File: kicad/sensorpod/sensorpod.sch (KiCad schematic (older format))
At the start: 48 parts, among them M1 MOTOR, P1 HEADER_(8_WAY), Q1 IRFML8244TRPBF

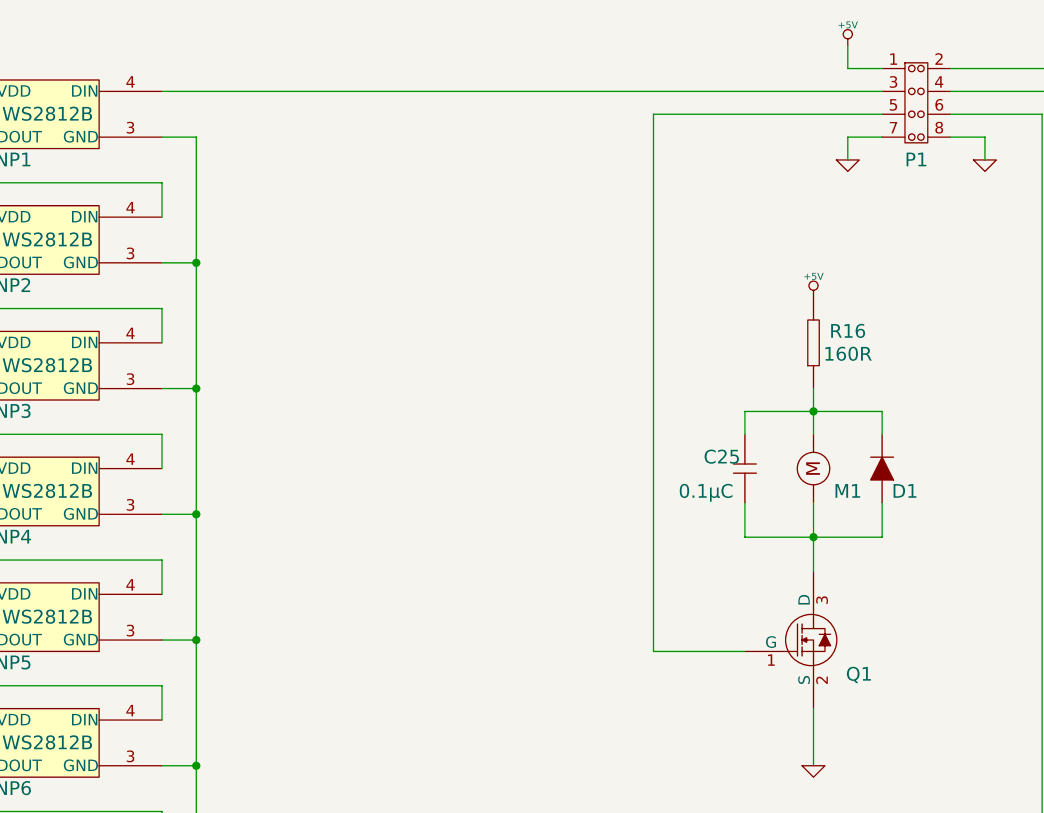
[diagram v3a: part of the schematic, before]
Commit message: Swap a few cable pins
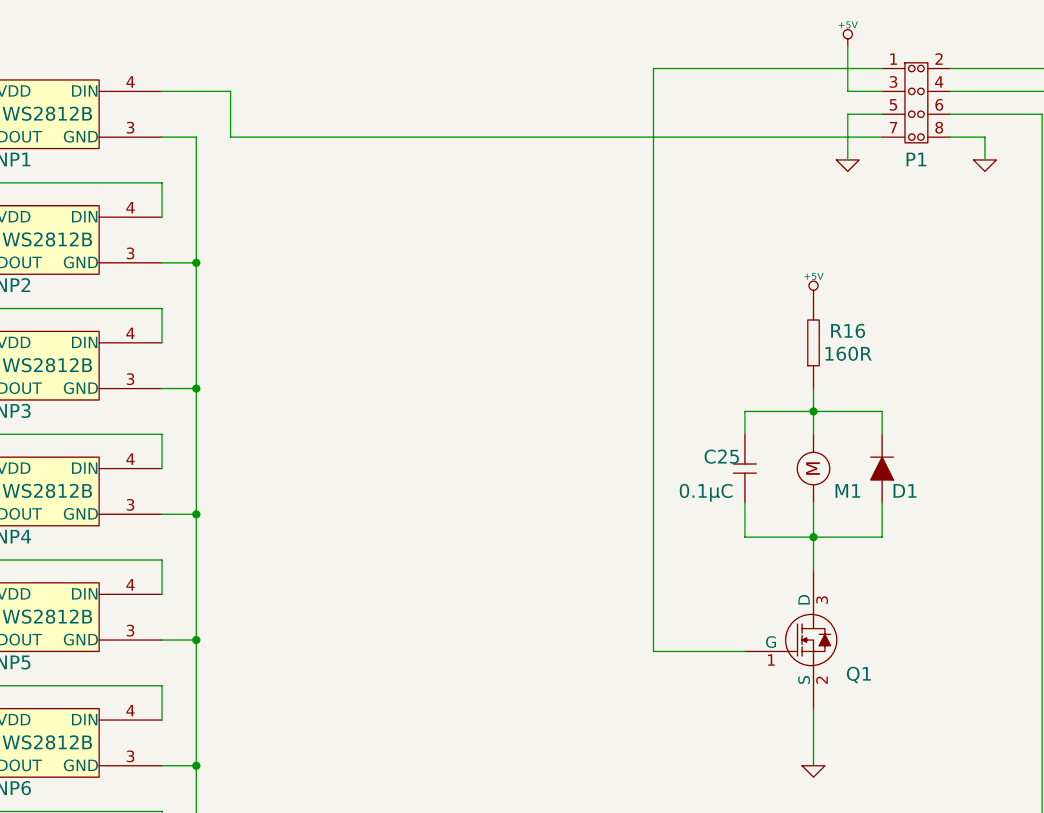
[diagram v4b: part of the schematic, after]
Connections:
- net +5V: now also P1.3; no longer P1.1
- net GND: now also P1.5; no longer P1.7
- net at NP1.4 (DIN): now also P1.7; no longer P1.3
- net at Q1.1 (G): now also P1.1; no longer P1.5
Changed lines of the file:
@@
 Sheet 1 1
 Title ""
-Date "22 feb 2016"
+Date "23 feb 2016"
 Rev ""
 Comp ""
@@
 	1    0    0    -1
 $EndComp
-Wire Wire Line
-	5300 900  5150 900
-Wire Wire Line
-	5150 900  5150 800
 $Comp
 L GND #PWR029
@@
 $EndComp
 Wire Wire Line
-	5600 1200 5750 1200
-Wire Wire Line
 	5750 1200 5750 1300
 Wire Wire Line
-	2150 1000 5300 1000
-Wire Wire Line
 	6100 4800 6100 1000
 Wire Wire Line
-	6100 1000 5600 1000
-Wire Wire Line
 	6000 4900 6000 1100
-Wire Wire Line
-	6000 1100 5600 1100
-Wire Wire Line
-	5600 900  6200 900
 Wire Wire Line
 	6200 900  6200 2500
@@
 $EndComp
 Wire Wire Line
-	5300 1200 5150 1200
-Wire Wire Line
-	5150 1200 5150 1300
+	5150 1100 5150 1300
 $Comp
 L IRFML8244TRPBF Q1
@@
 	5000 3700 5000 3950
 Wire Wire Line
-	4700 3450 4300 3450
-Wire Wire Line
-	4300 3450 4300 1100
-Wire Wire Line
-	4300 1100 5300 1100
+	4300 3450 4700 3450
+Wire Wire Line
+	4300 900  4300 3450
 $Comp
 L MOTOR M1
@@
 	7650 5350 7900 5350
 Connection ~ 7900 5350
+Wire Wire Line
+	4300 900  5300 900
+Wire Wire Line
+	5300 1000 5150 1000
+Wire Wire Line
+	5150 1000 5150 800
+Wire Wire Line
+	5150 1100 5300 1100
+Wire Wire Line
+	5300 1200 2450 1200
+Wire Wire Line
+	2450 1200 2450 1000
+Wire Wire Line
+	2450 1000 2150 1000
+Wire Wire Line
+	5600 1200 5750 1200
+Wire Wire Line
+	6000 1100 5600 1100
+Wire Wire Line
+	6100 1000 5600 1000
+Wire Wire Line
+	5600 900  6200 900
 $EndSCHEMATC

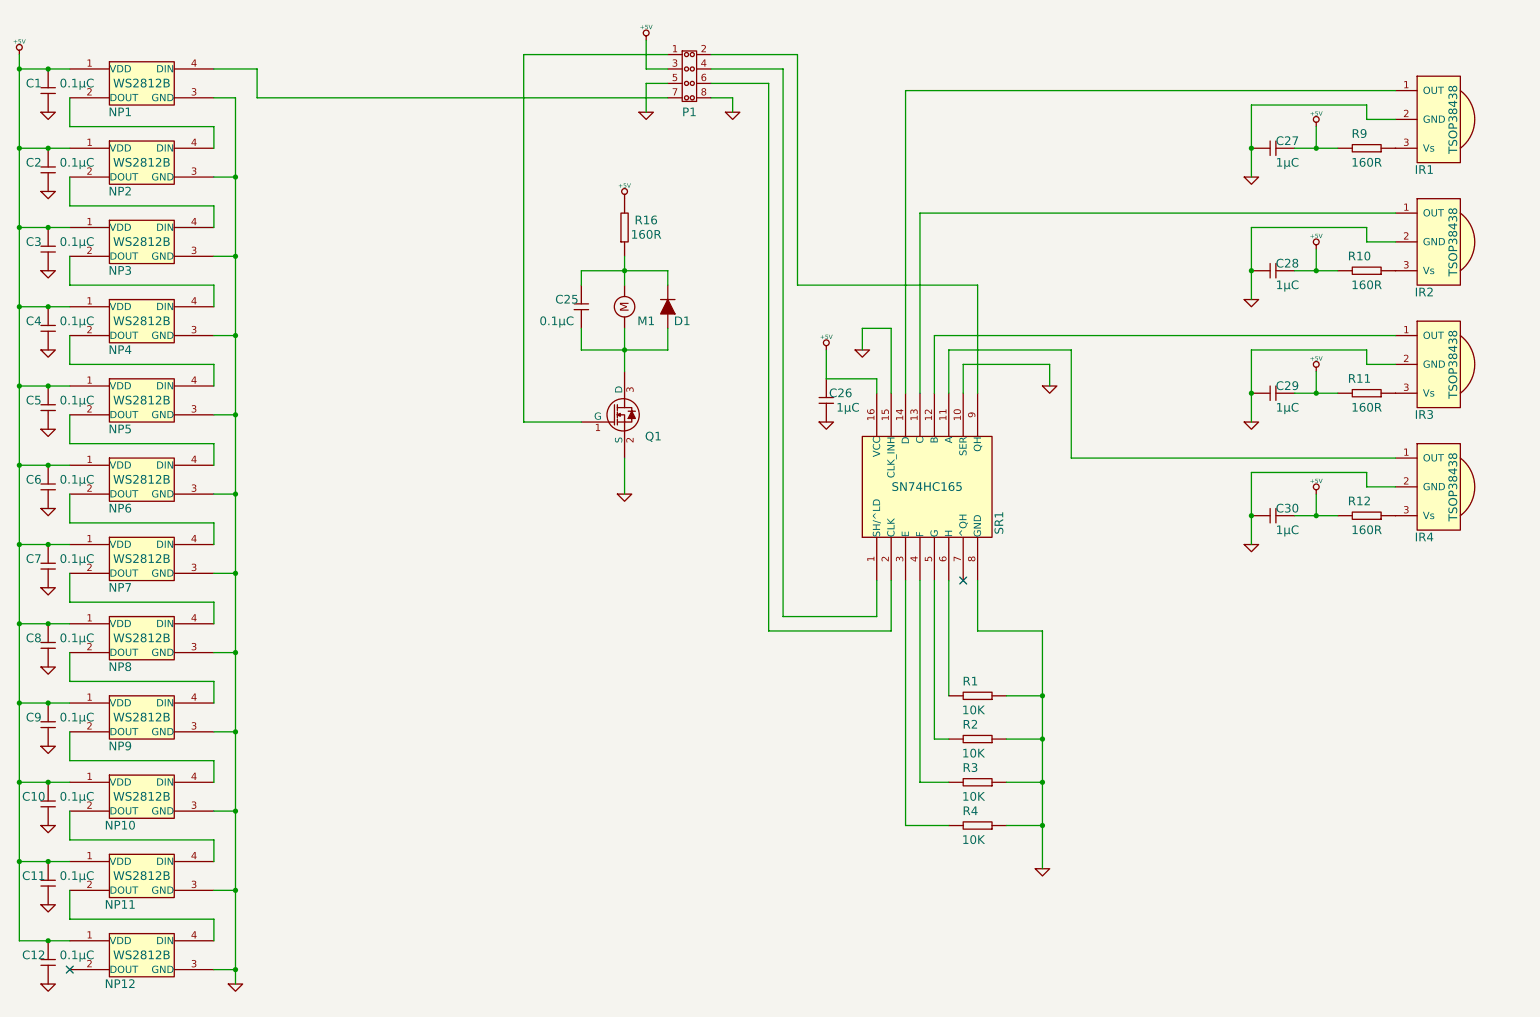
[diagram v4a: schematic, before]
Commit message: Updated sensorpod schematic and PCB to fit into Serpac C9 enclosure
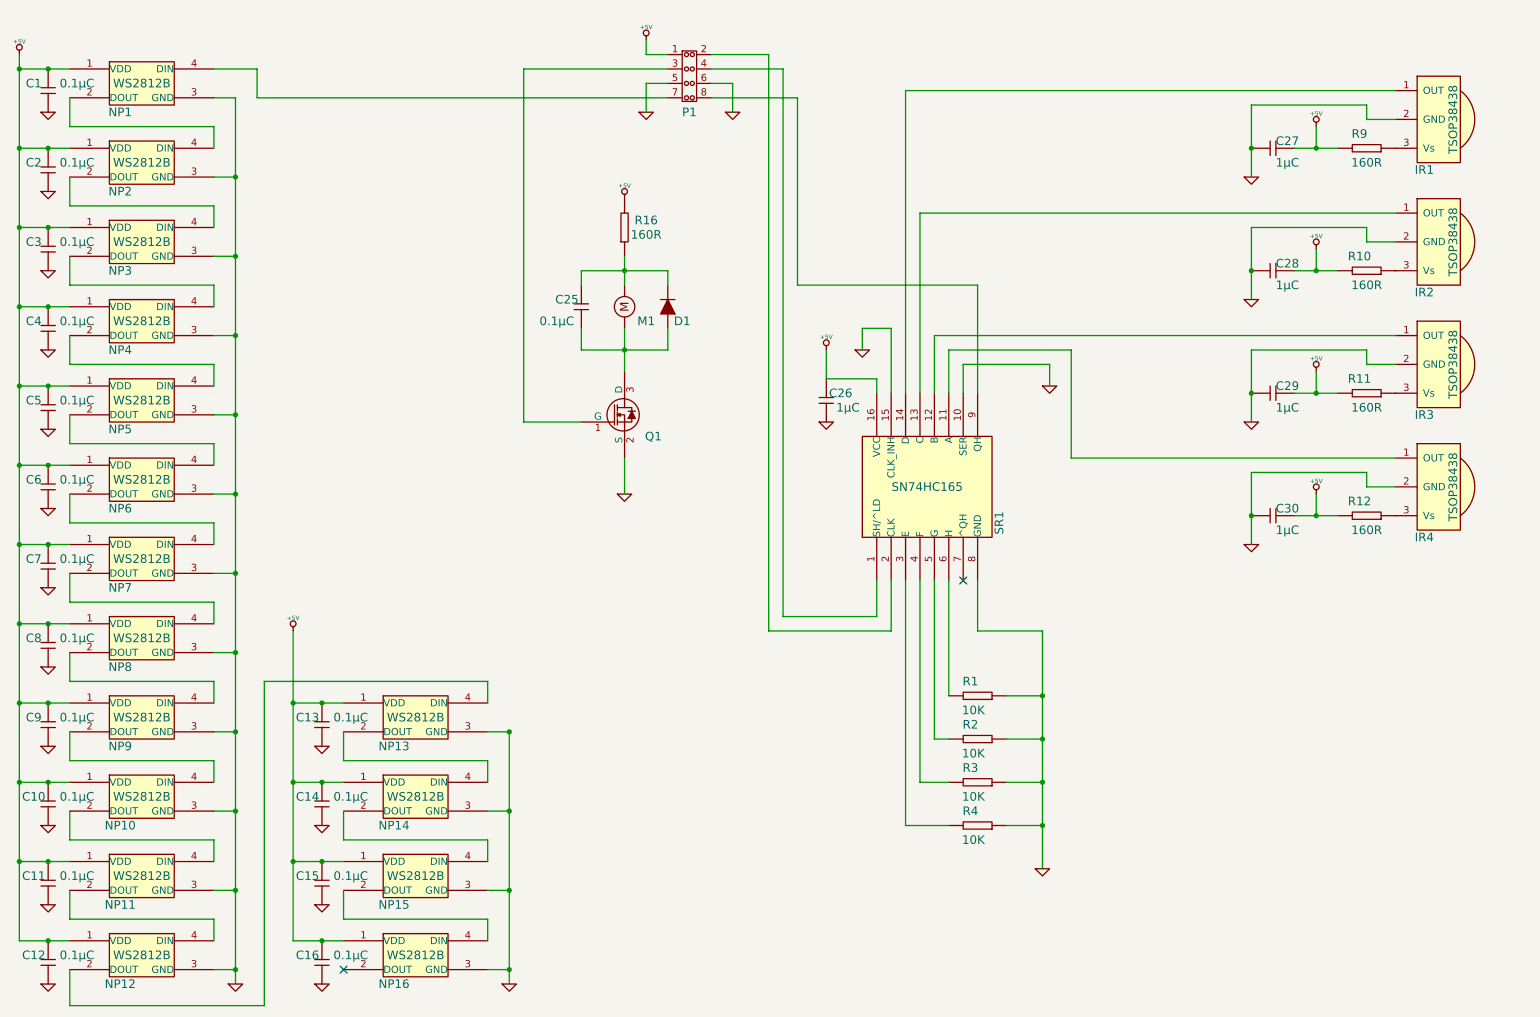
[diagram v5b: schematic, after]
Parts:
- added C13, C14, C15, C16: GENERIC_CAPACITOR, 0805, symbol GENERIC_CAPACITOR
- added NP13, NP14, NP15, NP16: WS2812B, 5050, symbol WS2812B
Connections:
- net +5V: now also P1.1, C13.1, C14.1, C15.1, C16.1, NP13.1 (VDD), NP14.1 (VDD), NP15.1 (VDD), NP16.1 (VDD); no longer P1.3
- net GND: now also P1.6, C13.2, C14.2, C15.2, C16.2, NP13.3 (GND), NP14.3 (GND), NP15.3 (GND), NP16.3 (GND); no longer P1.8
- net at NP12.2 (DOUT): now also NP13.4 (DIN)
- net at SR1.2 (CLK): now also P1.2; no longer P1.6
- net at SR1.9 (QH): now also P1.8; no longer P1.2
- net at Q1.1 (G): now also P1.3; no longer P1.1
- new net: NP13.2 (DOUT), NP14.4 (DIN)
- new net: NP14.2 (DOUT), NP15.4 (DIN)
- new net: NP15.2 (DOUT), NP16.4 (DIN)

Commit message: Remove vibration motor from sensor pos - it will just be in the command pod
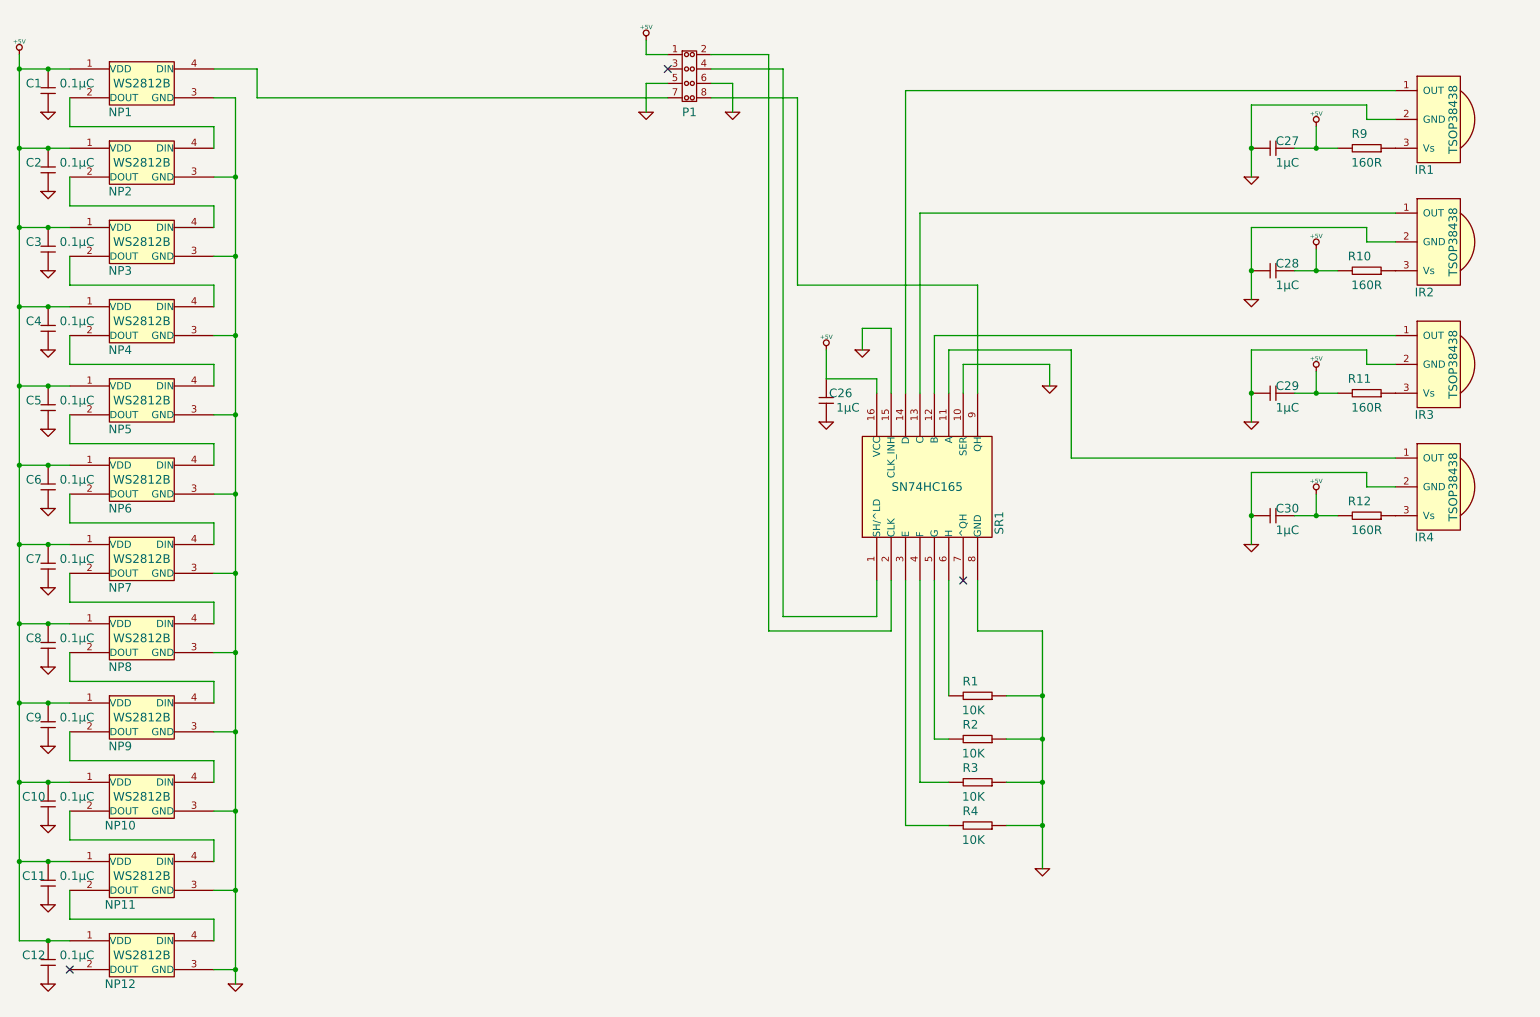
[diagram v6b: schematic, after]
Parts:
- removed C13, C14, C15, C16, C25: GENERIC_CAPACITOR, 0805, symbol GENERIC_CAPACITOR
- removed D1: GENERIC_DIODE, SOD-323, symbol GENERIC_DIODE
- removed M1: MOTOR, Header_2x1, symbol MOTOR
- removed NP13, NP14, NP15, NP16: WS2812B, 5050, symbol WS2812B
- removed Q1: IRFML8244TRPBF, SOT-23, symbol IRFML8244TRPBF
- removed R16: GENERIC_RESISTOR, 0805, symbol GENERIC_RESISTOR
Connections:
- no-connect marks 2 -> 3

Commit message: More stuff
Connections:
- net GND: now also P1.3; no longer P1.5
- net at NP1.4 (DIN): now also P1.4; no longer P1.7
- net at SR1.1 (SH/^LD): now also P1.7; no longer P1.4
- net at SR1.2 (CLK): now also P1.8; no longer P1.2
- net at SR1.9 (QH): now also P1.5; no longer P1.8
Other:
- moved on the sheet: C26
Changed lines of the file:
@@
 Sheet 1 1
 Title ""
-Date "29 feb 2016"
+Date "7 mar 2016"
 Rev ""
 Comp ""
@@
 L GENERIC_CAPACITOR C?
 U 1 1 56C300CE
-P 6400 3300
+P 6400 3400
 AR Path="/56BF0E3B/56C300CE" Ref="C?"  Part="1"
 AR Path="/56BF2119/56C300CE" Ref="C?"  Part="1"
 AR Path="/56C300CE" Ref="C26"  Part="1"
-F 0 "C26" V 6450 3200 60  0000 C CNN
-F 1 "GENERIC_CAPACITOR" H 6410 3100 60  0001 C CNN
-F 2 "0805" H 6370 3050 60  0001 C CNN
-F 3 "~" H 6370 3050 60  0000 C CNN
-F 4 "1µC" V 6350 3150 60  0000 C CNN "Capacitance"
-	1    6400 3300
+F 0 "C26" V 6450 3300 60  0000 C CNN
+F 1 "GENERIC_CAPACITOR" H 6410 3200 60  0001 C CNN
+F 2 "0805" H 6370 3150 60  0001 C CNN
+F 3 "~" H 6370 3150 60  0000 C CNN
+F 4 "1µC" V 6350 3250 60  0000 C CNN "Capacitance"
+	1    6400 3400
 	0    -1   -1   0
 $EndComp
@@
 L GND #PWR?
 U 1 1 56C318C7
-P 6400 3450
+P 6400 3650
 AR Path="/56BF0E3B/56C318C7" Ref="#PWR?"  Part="1"
 AR Path="/56BF2119/56C318C7" Ref="#PWR?"  Part="1"
 AR Path="/56C318C7" Ref="#PWR018"  Part="1"
-F 0 "#PWR018" H 6400 3450 30  0001 C CNN
-F 1 "GND" H 6400 3380 30  0001 C CNN
-F 2 "" H 6400 3450 60  0000 C CNN
-F 3 "" H 6400 3450 60  0000 C CNN
-	1    6400 3450
+F 0 "#PWR018" H 6400 3650 30  0001 C CNN
+F 1 "GND" H 6400 3580 30  0001 C CNN
+F 2 "" H 6400 3650 60  0000 C CNN
+F 3 "" H 6400 3650 60  0000 C CNN
+	1    6400 3650
 	1    0    0    -1
 $EndComp
@@
 Wire Wire Line
 	2150 1400 2150 1550
-Wire Wire Line
-	800  1000 1150 1000
 Connection ~ 1000 1000
 Wire Wire Line
@@
 	6650 2800 6650 2950
 Wire Wire Line
-	6750 3250 6750 3150
-Wire Wire Line
 	6750 3150 6400 3150
 Wire Wire Line
-	6400 3150 6400 2950
+	6400 2950 6400 3250
 Wire Wire Line
 	7350 3250 7350 3050
@@
 	6750 4800 6750 4550
 Wire Wire Line
-	6100 4800 6750 4800
+	5050 4800 6750 4800
 Wire Wire Line
 	6850 4900 6850 4550
 Wire Wire Line
-	6000 4900 6850 4900
+	5650 4900 6850 4900
 Wire Wire Line
 	10350 3900 10150 3900
@@
 	10150 1250 9350 1250
 Wire Wire Line
-	9350 1250 9350 1750
-Wire Wire Line
 	9650 1550 9950 1550
 Wire Wire Line
@@
 	5750 1100 5750 1300
 Wire Wire Line
-	6100 4800 6100 1000
-Wire Wire Line
-	6000 900  6000 4900
-Wire Wire Line
-	6200 1200 6200 2500
-Wire Wire Line
-	6200 2500 7450 2500
+	5250 2500 7450 2500
 Wire Wire Line
 	7450 2500 7450 3250
 Wire Wire Line
-	5150 1100 5150 1300
+	5150 1000 5150 1300
 Wire Wire Line
 	800  900  800  7050
@@
 	5150 900  5150 800
 Wire Wire Line
-	5150 1100 5300 1100
-Wire Wire Line
-	5300 1200 2450 1200
-Wire Wire Line
-	2450 1200 2450 1000
-Wire Wire Line
-	2450 1000 2150 1000
+	2150 1000 3550 1000
 Wire Wire Line
 	5150 900  5300 900
+NoConn ~ 1150 7250
+NoConn ~ 5600 900
+Wire Wire Line
+	5150 1000 5300 1000
+Wire Wire Line
+	5300 1100 5250 1100
 Wire Wire Line
 	5600 1100 5750 1100
 Wire Wire Line
-	6000 900  5600 900
-Wire Wire Line
-	6100 1000 5600 1000
-Wire Wire Line
-	6200 1200 5600 1200
-NoConn ~ 1150 7250
-NoConn ~ 5300 1000
+	5250 1100 5250 2500
+Wire Wire Line
+	5300 1200 5050 1200
+Wire Wire Line
+	5050 1200 5050 4800
+Wire Wire Line
+	5600 1200 5650 1200
+Wire Wire Line
+	5650 1200 5650 4900
+Wire Wire Line
+	5600 1000 5750 1000
+Wire Wire Line
+	5750 1000 5750 600
+Wire Wire Line
+	5750 600  3550 600
+Wire Wire Line
+	3550 600  3550 1000
+Wire Wire Line
+	800  1000 1150 1000
+Wire Wire Line
+	6400 3650 6400 3550
+Connection ~ 6400 3150
+Wire Wire Line
+	6750 3250 6750 3150
+Wire Wire Line
+	9350 1250 9350 1750
 $EndSCHEMATC
